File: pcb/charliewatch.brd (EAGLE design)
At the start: 33 x 33 mm, 85 parts, among them U2 CC430F5137IRGZR, X1 CRYSTALS-NOGND-IQXC-25, X2 FA-128

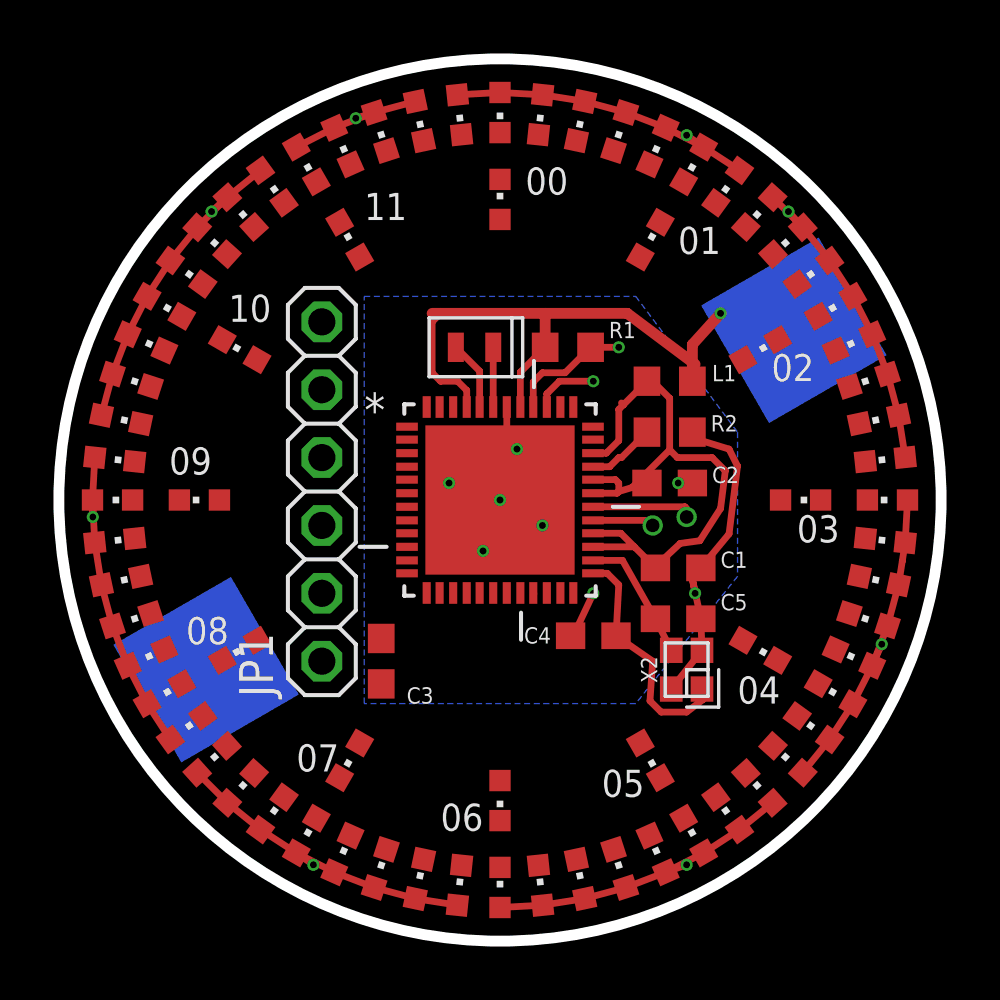
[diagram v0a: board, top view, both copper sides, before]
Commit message: move labels and 1x6 around; issues with the additional vcc line
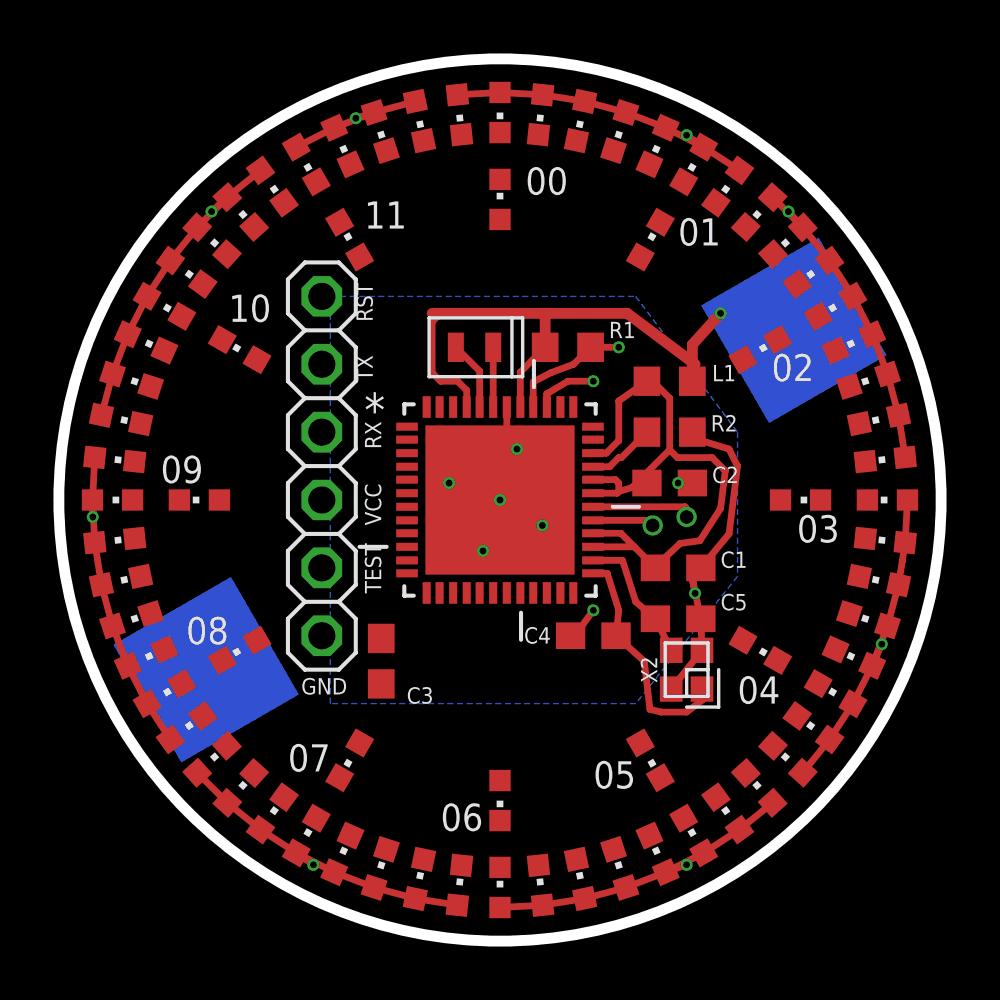
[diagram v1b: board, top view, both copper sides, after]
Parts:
- moved JP1 0.95 mm to (18.7, 26.7)
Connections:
- removed net DVCC_3: U2.22
- net BSL_VCC: now also U2.22
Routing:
- net GND: track 29.7 -> 29.2 mm
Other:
- board text added: "GND"
- board text added: "RST"
- board text added: "RX"
- board text added: "TEST"
- board text added: "TX"
- board text added: "VCC"
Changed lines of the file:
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@@
 <text x="27.94" y="39.37" size="0.8128" layer="26" font="vector" rot="MR330">https://trmm.net/Charliewatch</text>
 <text x="26.3525" y="36.83" size="1.016" layer="25" font="vector">00</text>
-<text x="32.0675" y="34.6075" size="1.016" layer="25" font="vector">01</text>
+<text x="32.0675" y="34.925" size="1.016" layer="25" font="vector">01</text>
 <text x="35.56" y="29.845" size="1.016" layer="25" font="vector">02</text>
 <text x="36.5125" y="23.8125" size="1.016" layer="25" font="vector">03</text>
 <text x="34.29" y="17.78" size="1.016" layer="25" font="vector">04</text>
-<text x="29.21" y="14.2875" size="1.016" layer="25" font="vector">05</text>
+<text x="28.8925" y="14.605" size="1.016" layer="25" font="vector">05</text>
 <text x="23.1775" y="13.0175" size="1.016" layer="25" font="vector">06</text>
-<text x="17.78" y="15.24" size="1.016" layer="25" font="vector">07</text>
+<text x="17.4625" y="15.24" size="1.016" layer="25" font="vector">07</text>
 <text x="13.6525" y="20.0025" size="1.016" layer="25" font="vector">08</text>
-<text x="13.0175" y="26.3525" size="1.016" layer="25" font="vector">09</text>
+<text x="12.7" y="26.035" size="1.016" layer="25" font="vector">09</text>
 <text x="15.24" y="32.0675" size="1.016" layer="25" font="vector">10</text>
-<text x="20.32" y="35.8775" size="1.016" layer="25" font="vector">11</text>
+<text x="20.32" y="35.56" size="1.016" layer="25" font="vector">11</text>
+<text x="19.685" y="18.7325" size="0.6096" layer="25" font="vector" rot="R180">GND</text>
+<text x="20.955" y="21.9075" size="0.6096" layer="25" font="vector" rot="R90">TEST</text>
+<text x="20.955" y="24.4475" size="0.6096" layer="25" font="vector" rot="R90">VCC</text>
+<text x="20.955" y="27.305" size="0.6096" layer="25" font="vector" rot="R90">RX</text>
+<text x="20.6375" y="29.845" size="0.6096" layer="25" font="vector" rot="R90">TX</text>
+<text x="20.6375" y="32.0675" size="0.6096" layer="25" font="vector" rot="R90">RST</text>
 </plain>
 <attributes>
@@
 <attribute name="VALUE" x="35.3145" y="16.863584375" size="1.6764" layer="28" font="vector" rot="MR330"/>
 </element>
-<element name="JP1" library="adafruit" package="1X06" value="" x="18.7325" y="25.7175" rot="R90"/>
+<element name="JP1" library="adafruit" package="1X06" value="" x="18.7325" y="26.67" smashed="yes" rot="R90">
+<attribute name="VALUE" x="21.9075" y="19.05" size="1.27" layer="27" rot="R90"/>
+</element>
 </elements>
 <signals>
@@
 <wire x1="32.96" y1="19.775" x2="32.9175" y2="20.955" width="0.254" layer="1"/>
 <wire x1="32.6" y1="22.44" x2="32.9175" y2="22.86" width="0.254" layer="1"/>
-<via x="28.8925" y="21.9075" extent="1-16" drill="0.254"/>
+<via x="28.8925" y="21.2725" extent="1-16" drill="0.254"/>
 <wire x1="28.0425" y1="20.32" x2="28.0425" y2="20.105" width="0.254" layer="1"/>
-<wire x1="28.0425" y1="20.105" x2="28.8925" y2="21.9075" width="0.254" layer="1"/>
+<wire x1="28.0425" y1="20.105" x2="28.8925" y2="21.2725" width="0.254" layer="1"/>
 <wire x1="32.6" y1="27.725" x2="32.805" y2="27.725" width="0.254" layer="1"/>
 <via x="32.0675" y="26.035" extent="1-16" drill="0.254"/>
@@
 <via x="23.495" y="26.035" extent="1-16" drill="0.254"/>
 <polygon width="0.254" layer="16">
-<vertex x="20.32" y="33.02"/>
+<vertex x="19.05" y="33.02"/>
 <vertex x="30.48" y="33.02"/>
 <vertex x="34.29" y="27.94"/>
 <vertex x="34.29" y="22.5425"/>
 <vertex x="30.48" y="17.78"/>
-<vertex x="20.32" y="17.78"/>
+<vertex x="19.05" y="17.78"/>
 </polygon>
 <wire x1="23.495" y1="26.035" x2="25.4" y2="25.4" width="0.254" layer="1"/>
@@
 <wire x1="33.9725" y1="24.13" x2="32.9175" y2="22.86" width="0.254" layer="1"/>
 <contactref element="JP1" pad="1"/>
-<wire x1="18.7325" y1="19.3675" x2="20.955" y2="18.5175" width="0" layer="19" extent="1-1"/>
-<wire x1="23.495" y1="23.1775" x2="20.955" y2="18.5175" width="0" layer="19" extent="1-1"/>
+<wire x1="18.7325" y1="20.32" x2="20.955" y2="18.5175" width="0" layer="19" extent="1-1"/>
 </signal>
 <signal name="VCC">
@@
 <contactref element="R1" pad="1"/>
 <wire x1="26.6446" y1="28.8798" x2="26.6446" y2="29.8196" width="0.254" layer="1"/>
-<wire x1="26.6446" y1="29.8196" x2="26.9875" y2="30.1625" width="0.254" layer="1"/>
-<wire x1="26.9875" y1="30.1625" x2="27.8375" y2="30.1625" width="0.254" layer="1"/>
-<wire x1="27.8375" y1="30.1625" x2="28.79" y2="31.115" width="0.254" layer="1"/>
+<wire x1="26.6446" y1="29.8196" x2="27.305" y2="30.1625" width="0.254" layer="1"/>
+<wire x1="27.305" y1="30.1625" x2="28.155" y2="30.48" width="0.254" layer="1"/>
+<wire x1="28.155" y1="30.48" x2="28.79" y2="31.115" width="0.254" layer="1"/>
 <via x="29.845" y="31.115" extent="1-16" drill="0.254"/>
 <wire x1="29.845" y1="31.115" x2="28.79" y2="31.115" width="0.254" layer="1"/>
 <contactref element="JP1" pad="6"/>
-<wire x1="18.7325" y1="32.0675" x2="26.6446" y2="29.8196" width="0" layer="19" extent="1-1"/>
+<wire x1="18.7325" y1="33.02" x2="26.6446" y2="29.8196" width="0" layer="19" extent="1-1"/>
 </signal>
 <signal name="BSL_TEST">
 <contactref element="U2" pad="39"/>
 <wire x1="27.1526" y1="28.8798" x2="27.1526" y2="29.3751" width="0.254" layer="1"/>
-<wire x1="27.1526" y1="29.3751" x2="27.6225" y2="29.845" width="0.254" layer="1"/>
-<wire x1="27.6225" y1="29.845" x2="28.8925" y2="29.845" width="0.254" layer="1"/>
+<wire x1="27.1526" y1="29.3751" x2="27.94" y2="29.845" width="0.254" layer="1"/>
+<wire x1="27.94" y1="29.845" x2="28.8925" y2="29.845" width="0.254" layer="1"/>
 <via x="28.8925" y="29.845" extent="1-16" drill="0.254"/>
 <contactref element="JP1" pad="2"/>
-<wire x1="18.7325" y1="21.9075" x2="27.1526" y2="28.8798" width="0" layer="19" extent="1-1"/>
+<wire x1="18.7325" y1="22.86" x2="27.1526" y2="28.8798" width="0" layer="19" extent="1-1"/>
 </signal>
 <signal name="BSL_RX">
 <contactref element="U2" pad="6"/>
 <contactref element="JP1" pad="4"/>
-<wire x1="18.7325" y1="26.9875" x2="21.9202" y2="25.654" width="0" layer="19" extent="1-1"/>
+<wire x1="18.7325" y1="27.94" x2="21.9202" y2="25.654" width="0" layer="19" extent="1-1"/>
 </signal>
 <signal name="BSL_TX">
 <contactref element="U2" pad="5"/>
 <contactref element="JP1" pad="5"/>
-<wire x1="18.7325" y1="29.5275" x2="21.9202" y2="26.162" width="0" layer="19" extent="1-1"/>
+<wire x1="21.9202" y1="26.162" x2="18.7325" y2="30.48" width="0" layer="19" extent="1-1"/>
 </signal>
 <signal name="XOUT">
@@
 <wire x1="28.8798" y1="27.1526" x2="29.3751" y2="27.1526" width="0.254" layer="1"/>
 <wire x1="29.3751" y1="27.1526" x2="29.845" y2="27.6225" width="0.254" layer="1"/>
-<wire x1="29.845" y1="27.6225" x2="29.845" y2="28.79" width="0.254" layer="1"/>
-<wire x1="29.845" y1="28.79" x2="30.0169" y2="28.9619" width="0.254" layer="1"/>
-<wire x1="30.0169" y1="28.9619" x2="30.9" y2="29.845" width="0.254" layer="1"/>
+<wire x1="29.845" y1="27.6225" x2="29.845" y2="29.1075" width="0.254" layer="1"/>
+<wire x1="29.845" y1="29.1075" x2="30.9" y2="29.845" width="0.254" layer="1"/>
 <wire x1="30.9" y1="26.035" x2="30.33965" y2="25.8663625" width="0.254" layer="1"/>
 <wire x1="30.33965" y1="25.8663625" x2="29.845" y2="25.7175" width="0.254" layer="1"/>
@@
 <wire x1="31.75" y1="27.2767125" x2="30.33965" y2="25.8663625" width="0.254" layer="1"/>
 <wire x1="32.8803" y1="23.876" x2="32.1437" y2="23.7744" width="0.254" layer="1"/>
-<wire x1="29.9466" y1="29.0322" x2="30.0169" y2="28.9619" width="0.254" layer="1"/>
 <wire x1="32.8803" y1="23.876" x2="33.655" y2="25.0825" width="0.254" layer="1"/>
 <wire x1="33.655" y1="25.0825" x2="33.8328" y2="26.4922" width="0.254" layer="1"/>
@@
 <contactref element="C4" pad="1"/>
 <wire x1="28.8798" y1="22.6568" x2="29.4132" y2="22.6568" width="0.254" layer="1"/>
-<wire x1="29.4132" y1="22.6568" x2="29.845" y2="22.225" width="0.254" layer="1"/>
-<wire x1="31.0125" y1="17.8825" x2="31.4325" y2="17.4625" width="0.254" layer="1"/>
+<wire x1="29.4132" y1="22.6568" x2="29.845" y2="21.2725" width="0.254" layer="1"/>
+<wire x1="31.0125" y1="17.565" x2="31.4325" y2="17.4625" width="0.254" layer="1"/>
 <wire x1="31.4325" y1="17.4625" x2="32.385" y2="17.4625" width="0.254" layer="1"/>
 <wire x1="32.385" y1="17.4625" x2="33.02" y2="17.9475" width="0.254" layer="1"/>
 <wire x1="33.02" y1="17.9475" x2="32.96" y2="18.325" width="0.254" layer="1"/>
-<wire x1="29.845" y1="22.225" x2="29.7425" y2="20.32" width="0.254" layer="1"/>
-<wire x1="29.7425" y1="20.32" x2="31.115" y2="19.3675" width="0.254" layer="1"/>
-<wire x1="31.115" y1="19.3675" x2="31.0125" y2="17.8825" width="0.254" layer="1"/>
+<wire x1="29.845" y1="21.2725" x2="29.7425" y2="20.32" width="0.254" layer="1"/>
+<wire x1="29.7425" y1="20.32" x2="30.7975" y2="19.3675" width="0.254" layer="1"/>
+<wire x1="30.7975" y1="19.3675" x2="31.0125" y2="17.565" width="0.254" layer="1"/>
 </signal>
 <signal name="RF_P">
@@
 <contactref element="C5" pad="1"/>
 <wire x1="28.8798" y1="23.1394" x2="29.9856" y2="23.1394" width="0.254" layer="1"/>
-<wire x1="29.9856" y1="23.1394" x2="31.2175" y2="20.955" width="0.254" layer="1"/>
+<wire x1="29.9856" y1="23.1394" x2="30.48" y2="21.59" width="0.254" layer="1"/>
+<wire x1="30.48" y1="21.59" x2="31.2175" y2="20.955" width="0.254" layer="1"/>
 <wire x1="31.2175" y1="20.955" x2="31.81" y2="19.775" width="0.254" layer="1"/>
 </signal>
@@
 <contactref element="U2" pad="14"/>
 </signal>
-<signal name="DVCC_3">
-<contactref element="U2" pad="22"/>
-</signal>
 <signal name="P2.4">
 <contactref element="U2" pad="47"/>
@@
 <contactref element="U2" pad="8"/>
 <contactref element="JP1" pad="3"/>
-<wire x1="18.7325" y1="24.4475" x2="21.9202" y2="24.638" width="0" layer="19" extent="1-1"/>
+<contactref element="U2" pad="22"/>
+<wire x1="21.9202" y1="24.638" x2="27.1526" y2="21.9202" width="0" layer="19" extent="1-1"/>
+<wire x1="18.7325" y1="25.4" x2="21.9202" y2="24.638" width="0" layer="19" extent="1-1"/>
 </signal>
 </signals>
+<errors>
+</errors>
 </board>
 </drawing>

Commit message: replace with "1x6 lock" part
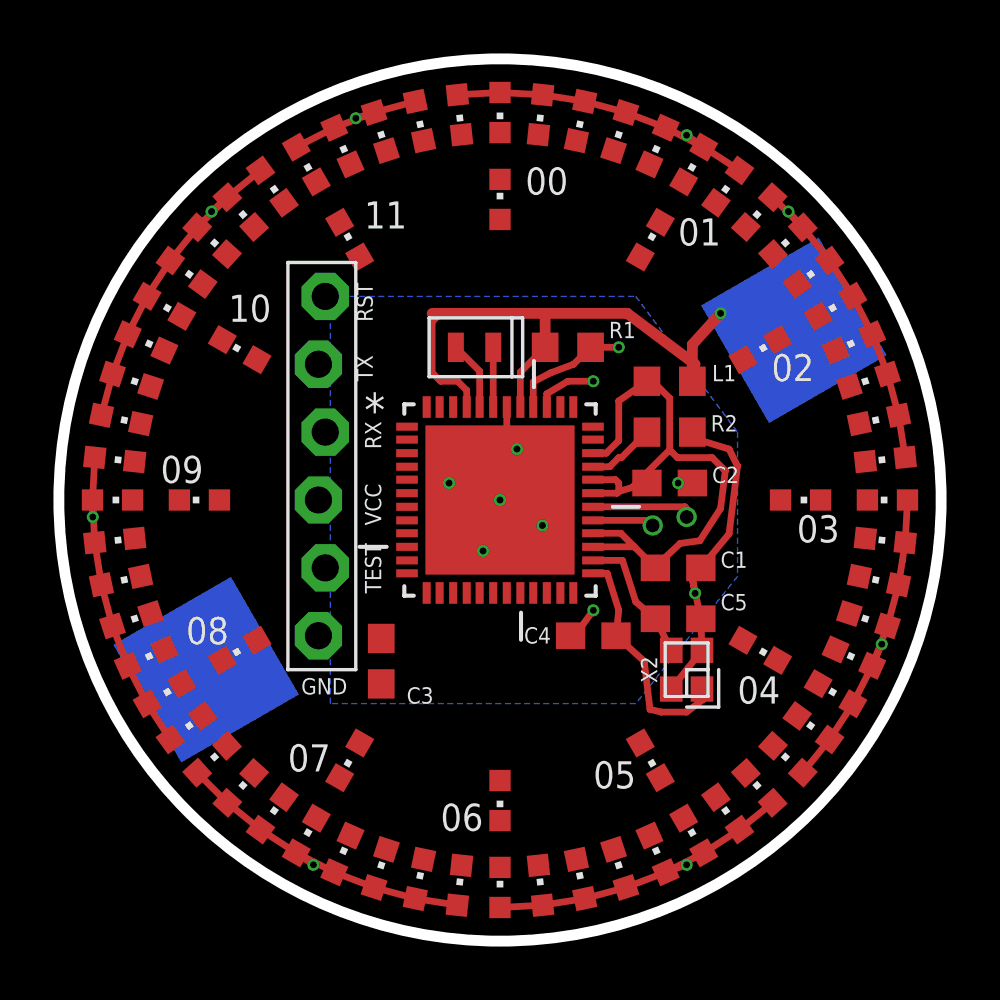
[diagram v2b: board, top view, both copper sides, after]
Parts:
- JP1: device adafruit:1X06 -> adafruit:1X06-BIGLOCK
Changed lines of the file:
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@@
 <attribute name="VALUE" x="35.3145" y="16.863584375" size="1.6764" layer="28" font="vector" rot="MR330"/>
 </element>
-<element name="JP1" library="adafruit" package="1X06" value="" x="18.7325" y="26.67" smashed="yes" rot="R90">
+<element name="JP1" library="adafruit" package="1X06-BIGLOCK" value="" x="18.7325" y="26.67" smashed="yes" rot="R90">
 <attribute name="VALUE" x="21.9075" y="19.05" size="1.27" layer="27" rot="R90"/>
 </element>
@@
 <wire x1="33.9725" y1="24.13" x2="32.9175" y2="22.86" width="0.254" layer="1"/>
 <contactref element="JP1" pad="1"/>
-<wire x1="18.7325" y1="20.32" x2="20.955" y2="18.5175" width="0" layer="19" extent="1-1"/>
+<wire x1="18.6055" y1="20.32" x2="20.955" y2="18.5175" width="0" layer="19" extent="1-1"/>
 </signal>
 <signal name="VCC">
@@
 <wire x1="29.845" y1="31.115" x2="28.79" y2="31.115" width="0.254" layer="1"/>
 <contactref element="JP1" pad="6"/>
-<wire x1="18.7325" y1="33.02" x2="26.6446" y2="29.8196" width="0" layer="19" extent="1-1"/>
+<wire x1="18.8595" y1="33.02" x2="26.6446" y2="29.8196" width="0" layer="19" extent="1-1"/>
 </signal>
 <signal name="BSL_TEST">
@@
 <via x="28.8925" y="29.845" extent="1-16" drill="0.254"/>
 <contactref element="JP1" pad="2"/>
-<wire x1="18.7325" y1="22.86" x2="27.1526" y2="28.8798" width="0" layer="19" extent="1-1"/>
+<wire x1="18.8595" y1="22.86" x2="27.1526" y2="28.8798" width="0" layer="19" extent="1-1"/>
 </signal>
 <signal name="BSL_RX">
 <contactref element="U2" pad="6"/>
 <contactref element="JP1" pad="4"/>
-<wire x1="18.7325" y1="27.94" x2="21.9202" y2="25.654" width="0" layer="19" extent="1-1"/>
+<wire x1="18.8595" y1="27.94" x2="21.9202" y2="25.654" width="0" layer="19" extent="1-1"/>
 </signal>
 <signal name="BSL_TX">
 <contactref element="U2" pad="5"/>
 <contactref element="JP1" pad="5"/>
-<wire x1="21.9202" y1="26.162" x2="18.7325" y2="30.48" width="0" layer="19" extent="1-1"/>
+<wire x1="21.9202" y1="26.162" x2="18.6055" y2="30.48" width="0" layer="19" extent="1-1"/>
 </signal>
 <signal name="XOUT">
@@
 <contactref element="U2" pad="22"/>
 <wire x1="21.9202" y1="24.638" x2="27.1526" y2="21.9202" width="0" layer="19" extent="1-1"/>
-<wire x1="18.7325" y1="25.4" x2="21.9202" y2="24.638" width="0" layer="19" extent="1-1"/>
+<wire x1="18.6055" y1="25.4" x2="21.9202" y2="24.638" width="0" layer="19" extent="1-1"/>
 </signal>
 </signals>
